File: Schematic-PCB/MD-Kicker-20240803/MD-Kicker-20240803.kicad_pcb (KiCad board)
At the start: 2 copper layers, 100.5 x 117.7 mm, 71 parts, among them J1 Conn_01x02_Pin, J2 Conn_01x04_Pin, J3 Conn_01x15_Pin, J4 Conn_01x02_Pin, J5 Conn_01x02_Pin, J6 Conn_01x02_Pin, J7 Conn_01x02_Pin, J8 Conn_01x02_Pin, Q1 NMOS, Q2 NMOS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

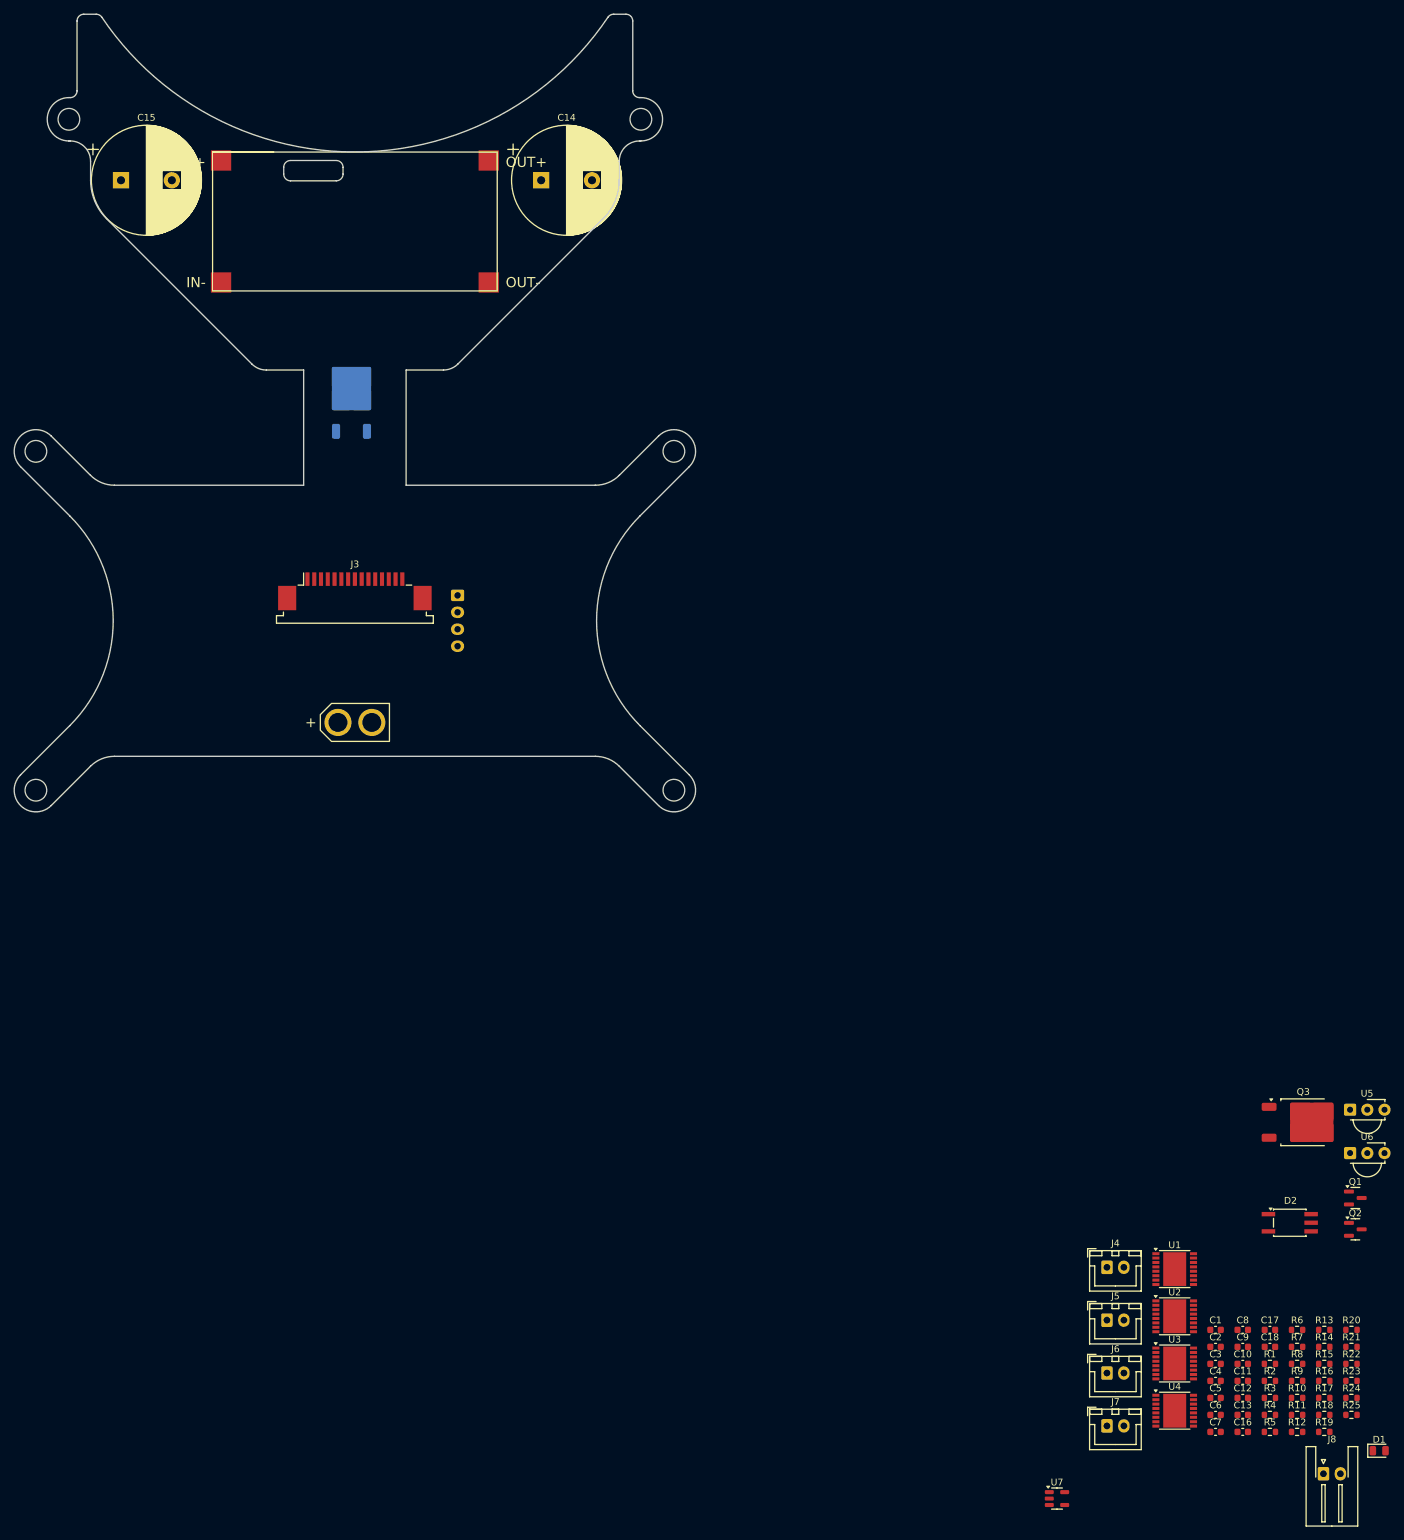
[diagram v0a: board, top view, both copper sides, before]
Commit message: キッカー基板を更新した
MDとの接続をピンヘッダ/ピンソケットを使う方式に変更した
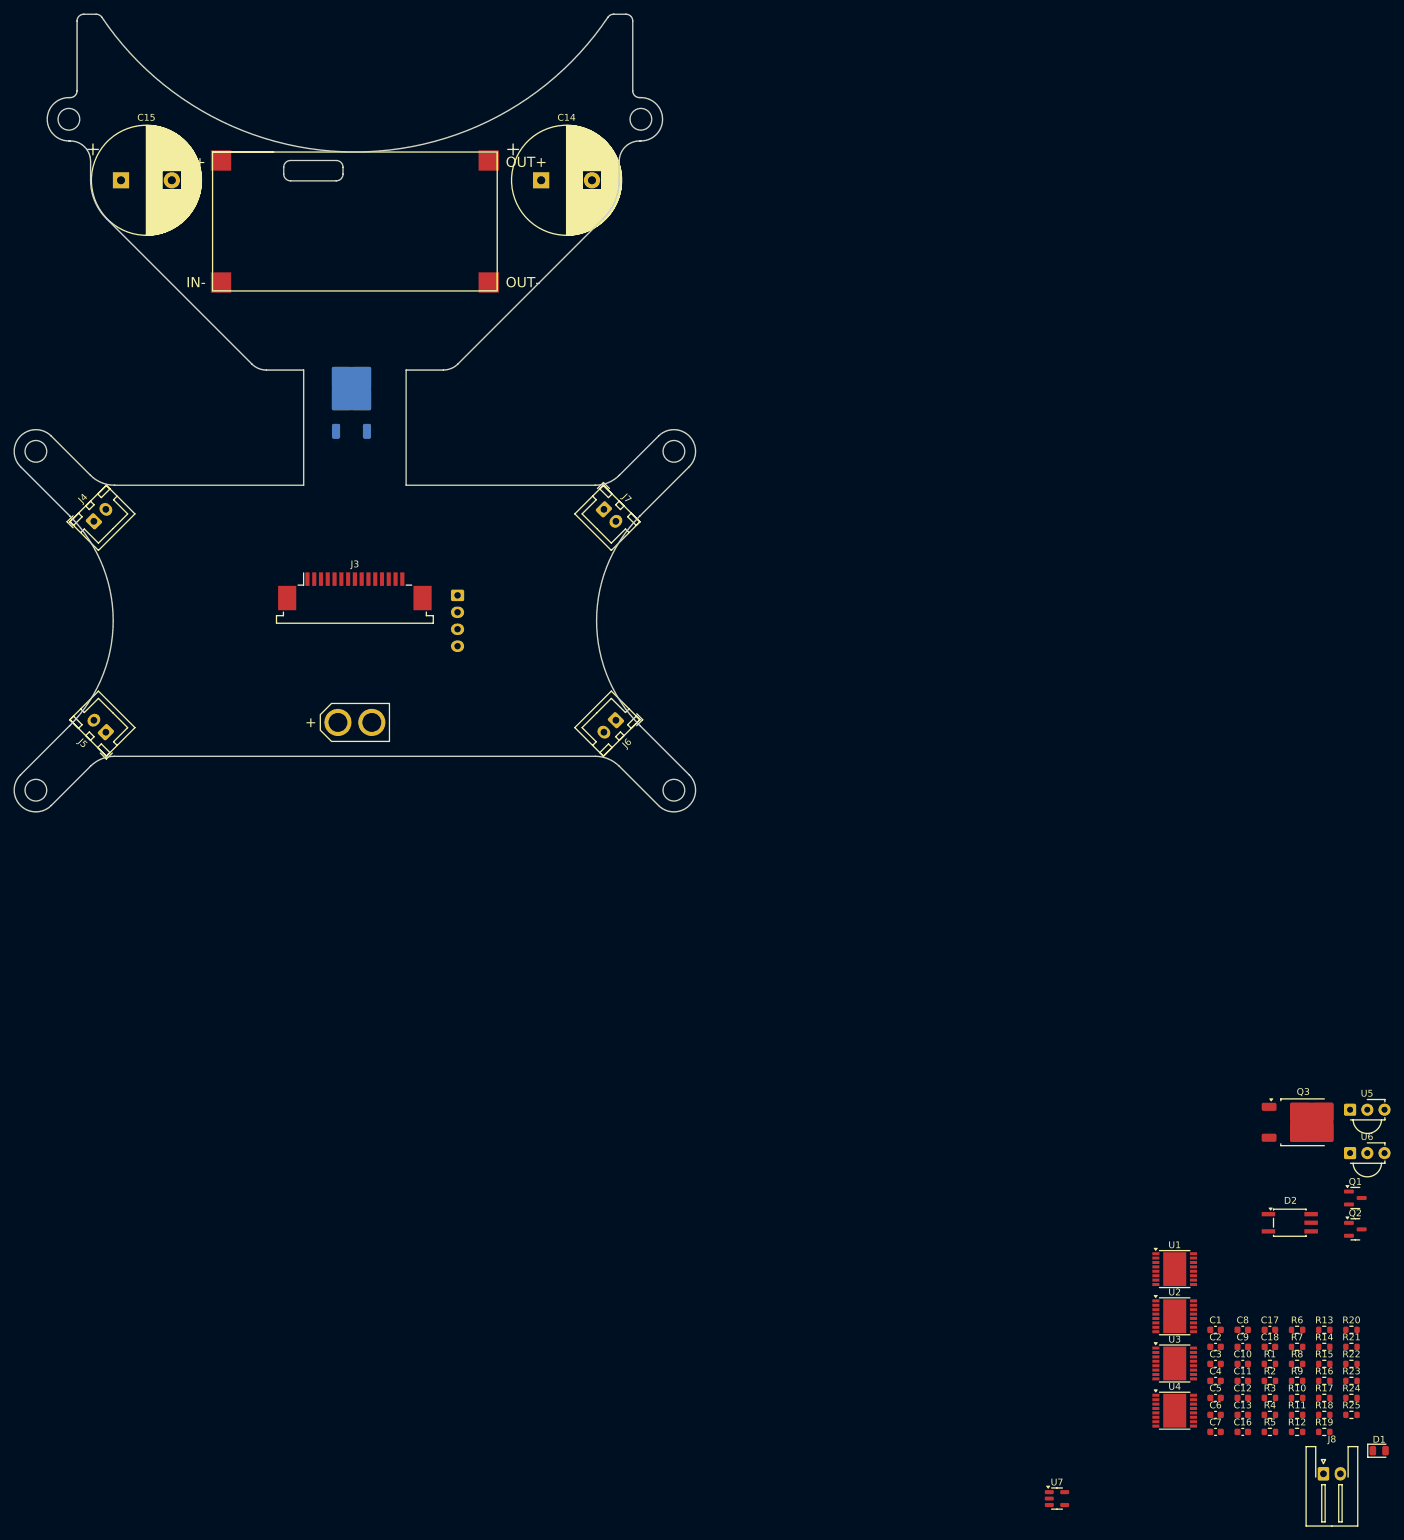
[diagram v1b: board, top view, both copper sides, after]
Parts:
- moved J4 186.5 mm to (-37.6, -15.6), turned to 45 degrees
- moved J5 173.6 mm to (-37.6, 15.6), turned to 135 degrees
- moved J7 153.7 mm to (37.6, -15.6), turned to -45 degrees
- moved J6 121.1 mm to (37.6, 15.6), turned to -135 degrees
